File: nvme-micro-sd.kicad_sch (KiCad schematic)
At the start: 31 parts, among them J6 MicroSD_1140084168, J7 Bus_M.2_1-2199230-6, M2 Mech_M2_2280_H2.5mm

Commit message: [#54617] Review requested changes
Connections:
- net GND: no longer J6.10 (CD2), R?.1, R?.1
- new net: J6.10 (CD2), R?.1, R?.1
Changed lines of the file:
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@@
     (comment 1 "www.antmicro.com")
   )
-  (junction (at 236.22 222.25) (diameter 0) (color 0 0 0 0)
-  )
   (junction (at 224.79 46.99) (diameter 0) (color 0 0 0 0)
   )
@@
     (stroke (width 0) (type default))
   )
-  (wire (pts (xy 236.22 222.25) (xy 236.22 224.79))
-    (stroke (width 0) (type default))
-  )
   (wire (pts (xy 217.17 59.69) (xy 220.98 59.69))
     (stroke (width 0) (type default))
@@
     (stroke (width 0) (type default))
   )
-  (wire (pts (xy 236.22 212.09) (xy 236.22 222.25))
+  (wire (pts (xy 236.22 212.09) (xy 236.22 224.79))
     (stroke (width 0) (type default))
   )
@@
     (stroke (width 0) (type default))
   )
-  (wire (pts (xy 237.49 222.25) (xy 236.22 222.25))
-    (stroke (width 0) (type default))
-  )
   (wire (pts (xy 204.47 124.46) (xy 203.2 124.46))
     (stroke (width 0) (type default))
@@
     (stroke (width 0) (type default))
   )
-  (wire (pts (xy 228.6 222.25) (xy 236.22 222.25))
+  (wire (pts (xy 228.6 222.25) (xy 237.49 222.25))
     (stroke (width 0) (type default))
   )
@@
       (effects (font (size 1.27 1.27) (thickness 0.15)) (justify left bottom) hide)
     )
-    (property "Datasheet" " " (at 284.48 177.8 0)
+    (property "Datasheet" "https://product.tdk.com/en/search/capacitor/ceramic/mlcc/info?part_no=C1005X6S1A105K050BC" (at 284.48 177.8 0)
       (effects (font (size 1.27 1.27) (thickness 0.15)) (justify left bottom) hide)
     )
@@
   (symbol (lib_id "antmicropower:+3V3") (at 203.2 185.42 0) (unit 1)
     (in_bom yes) (on_board yes) (dnp no) (fields_autoplaced)
-    (property "Reference" "#PWR?" (at 218.44 187.96 0)
+    (property "Reference" "#PWR0206" (at 218.44 187.96 0)
       (effects (font (size 1.27 1.27) (thickness 0.15)) (justify left bottom) hide)
     )
@@
       (project "cm4-baseboard"
         (path "/60b842dc-0853-4a25-99ac-5784ddf94d0d/00000000-0000-0000-0000-00005fea1b94"
-          (reference "#PWR?") (unit 1)
+          (reference "#PWR0206") (unit 1)
         )
       )
@@
   (symbol (lib_id "antmicropower:GND") (at 269.24 199.39 0) (unit 1)
     (in_bom yes) (on_board yes) (dnp no)
-    (property "Reference" "#PWR?" (at 278.13 201.93 0)
+    (property "Reference" "#PWR0213" (at 278.13 201.93 0)
       (effects (font (size 1.27 1.27) (thickness 0.15)) (justify left bottom) hide)
     )
@@
       (project "cm4-baseboard"
         (path "/60b842dc-0853-4a25-99ac-5784ddf94d0d/00000000-0000-0000-0000-00005fea1b94"
-          (reference "#PWR?") (unit 1)
+          (reference "#PWR0213") (unit 1)
         )
       )
@@
       (effects (font (size 1.524 1.524)) (justify left bottom) hide)
     )
-    (property "Datasheet" " " (at 260.35 54.61 0)
+    (property "Datasheet" "https://product.tdk.com/en/search/capacitor/ceramic/mlcc/info?part_no=C1005X6S1A105K050BC" (at 260.35 54.61 0)
       (effects (font (size 1.27 1.27)) (justify left bottom) hide)
     )
@@
   (symbol (lib_id "antmicropower:+3V3") (at 236.22 185.42 0) (unit 1)
     (in_bom yes) (on_board yes) (dnp no) (fields_autoplaced)
-    (property "Reference" "#PWR?" (at 251.46 187.96 0)
+    (property "Reference" "#PWR0207" (at 251.46 187.96 0)
       (effects (font (size 1.27 1.27) (thickness 0.15)) (justify left bottom) hide)
     )
@@
       (project "cm4-baseboard"
         (path "/60b842dc-0853-4a25-99ac-5784ddf94d0d/00000000-0000-0000-0000-00005fea1b94"
-          (reference "#PWR?") (unit 1)
+          (reference "#PWR0207") (unit 1)
         )
       )
@@
   (symbol (lib_id "antmicropower:GND") (at 261.62 224.79 0) (unit 1)
     (in_bom yes) (on_board yes) (dnp no) (fields_autoplaced)
-    (property "Reference" "#PWR?" (at 270.51 227.33 0)
+    (property "Reference" "#PWR0212" (at 270.51 227.33 0)
       (effects (font (size 1.27 1.27) (thickness 0.15)) (justify left bottom) hide)
     )
@@
       (project "cm4-baseboard"
         (path "/60b842dc-0853-4a25-99ac-5784ddf94d0d/00000000-0000-0000-0000-00005fea1b94"
-          (reference "#PWR?") (unit 1)
+          (reference "#PWR0212") (unit 1)
         )
       )
@@
   (symbol (lib_id "antmicropower:GND") (at 151.13 210.82 0) (mirror y) (unit 1)
     (in_bom yes) (on_board yes) (dnp no) (fields_autoplaced)
-    (property "Reference" "#PWR?" (at 142.24 213.36 0)
+    (property "Reference" "#PWR0210" (at 142.24 213.36 0)
       (effects (font (size 1.27 1.27) (thickness 0.15)) (justify left bottom) hide)
     )
@@
       (project "cm4-baseboard"
         (path "/60b842dc-0853-4a25-99ac-5784ddf94d0d/00000000-0000-0000-0000-00005fea1b94"
-          (reference "#PWR?") (unit 1)
+          (reference "#PWR0210") (unit 1)
         )
       )
@@
       (effects (font (size 1.524 1.524)) (justify left bottom) hide)
     )
-    (property "Datasheet" " " (at 242.57 54.61 0)
+    (property "Datasheet" "https://product.tdk.com/en/search/capacitor/ceramic/mlcc/info?part_no=C1005X6S1A105K050BC" (at 242.57 54.61 0)
       (effects (font (size 1.27 1.27)) (justify left bottom) hide)
     )
@@
   (symbol (lib_id "antmicropower:GND") (at 228.6 231.14 0) (unit 1)
     (in_bom yes) (on_board yes) (dnp no) (fields_autoplaced)
-    (property "Reference" "#PWR?" (at 237.49 233.68 0)
+    (property "Reference" "#PWR0211" (at 237.49 233.68 0)
       (effects (font (size 1.27 1.27) (thickness 0.15)) (justify left bottom) hide)
     )
@@
       (project "cm4-baseboard"
         (path "/60b842dc-0853-4a25-99ac-5784ddf94d0d/00000000-0000-0000-0000-00005fea1b94"
-          (reference "#PWR?") (unit 1)
+          (reference "#PWR0211") (unit 1)
         )
       )
@@
       (effects (font (size 1.524 1.524)) (justify left bottom) hide)
     )
-    (property "Datasheet" " " (at 224.79 54.61 0)
+    (property "Datasheet" "https://product.tdk.com/en/search/capacitor/ceramic/mlcc/info?part_no=C1005X6S1A105K050BC" (at 224.79 54.61 0)
       (effects (font (size 1.27 1.27)) (justify left bottom) hide)
     )
@@
   (symbol (lib_id "antmicropower:+3V3") (at 151.13 195.58 0) (mirror y) (unit 1)
     (in_bom yes) (on_board yes) (dnp no) (fields_autoplaced)
-    (property "Reference" "#PWR?" (at 135.89 198.12 0)
+    (property "Reference" "#PWR0205" (at 135.89 198.12 0)
       (effects (font (size 1.27 1.27) (thickness 0.15)) (justify left bottom) hide)
     )
@@
       (project "cm4-baseboard"
         (path "/60b842dc-0853-4a25-99ac-5784ddf94d0d/00000000-0000-0000-0000-00005fea1b94"
-          (reference "#PWR?") (unit 1)
+          (reference "#PWR0205") (unit 1)
         )
       )
@@
       (effects (font (size 1.27 1.27) (thickness 0.15)) (justify left bottom) hide)
     )
-    (property "Datasheet" "https://pl.mouser.com/datasheet/2/916/PUSB3F96-1600324.pdf" (at 124.46 212.09 0)
+    (property "Datasheet" "https://mouser.com/datasheet/2/916/PUSB3F96-1600324.pdf" (at 124.46 212.09 0)
       (effects (font (size 1.27 1.27) (thickness 0.15)) (justify left bottom) hide)
     )
@@
       (effects (font (size 1.27 1.27) (thickness 0.15)) (justify left bottom) hide)
     )
-    (property "Datasheet" "https://pl.mouser.com/datasheet/2/916/PUSB3F96-1600324.pdf" (at 124.46 234.95 0)
+    (property "Datasheet" "https://mouser.com/datasheet/2/916/PUSB3F96-1600324.pdf" (at 124.46 234.95 0)
       (effects (font (size 1.27 1.27) (thickness 0.15)) (justify left bottom) hide)
     )
@@
   (symbol (lib_id "antmicropower:GND") (at 266.7 121.92 0) (mirror y) (unit 1)
     (in_bom yes) (on_board yes) (dnp no) (fields_autoplaced)
-    (property "Reference" "#PWR?" (at 257.81 124.46 0)
+    (property "Reference" "#PWR0208" (at 257.81 124.46 0)
       (effects (font (size 1.27 1.27) (thickness 0.15)) (justify left bottom) hide)
     )
@@
       (project "cm4-baseboard"
         (path "/60b842dc-0853-4a25-99ac-5784ddf94d0d/00000000-0000-0000-0000-00005fea1b94"
-          (reference "#PWR?") (unit 1)
+          (reference "#PWR0208") (unit 1)
         )
       )
@@
   (symbol (lib_id "antmicropower:GND") (at 151.13 233.68 0) (mirror y) (unit 1)
     (in_bom yes) (on_board yes) (dnp no) (fields_autoplaced)
-    (property "Reference" "#PWR?" (at 142.24 236.22 0)
+    (property "Reference" "#PWR0209" (at 142.24 236.22 0)
       (effects (font (size 1.27 1.27) (thickness 0.15)) (justify left bottom) hide)
     )
@@
       (project "cm4-baseboard"
         (path "/60b842dc-0853-4a25-99ac-5784ddf94d0d/00000000-0000-0000-0000-00005fea1b94"
-          (reference "#PWR?") (unit 1)
+          (reference "#PWR0209") (unit 1)
         )
       )
@@
   (symbol (lib_id "antmicropower:+3V3") (at 269.24 191.77 0) (unit 1)
     (in_bom yes) (on_board yes) (dnp no) (fields_autoplaced)
-    (property "Reference" "#PWR?" (at 284.48 194.31 0)
+    (property "Reference" "#PWR0214" (at 284.48 194.31 0)
       (effects (font (size 1.27 1.27) (thickness 0.15)) (justify left bottom) hide)
     )
@@
       (project "cm4-baseboard"
         (path "/60b842dc-0853-4a25-99ac-5784ddf94d0d/00000000-0000-0000-0000-00005fea1b94"
-          (reference "#PWR?") (unit 1)
+          (reference "#PWR0214") (unit 1)
         )
       )

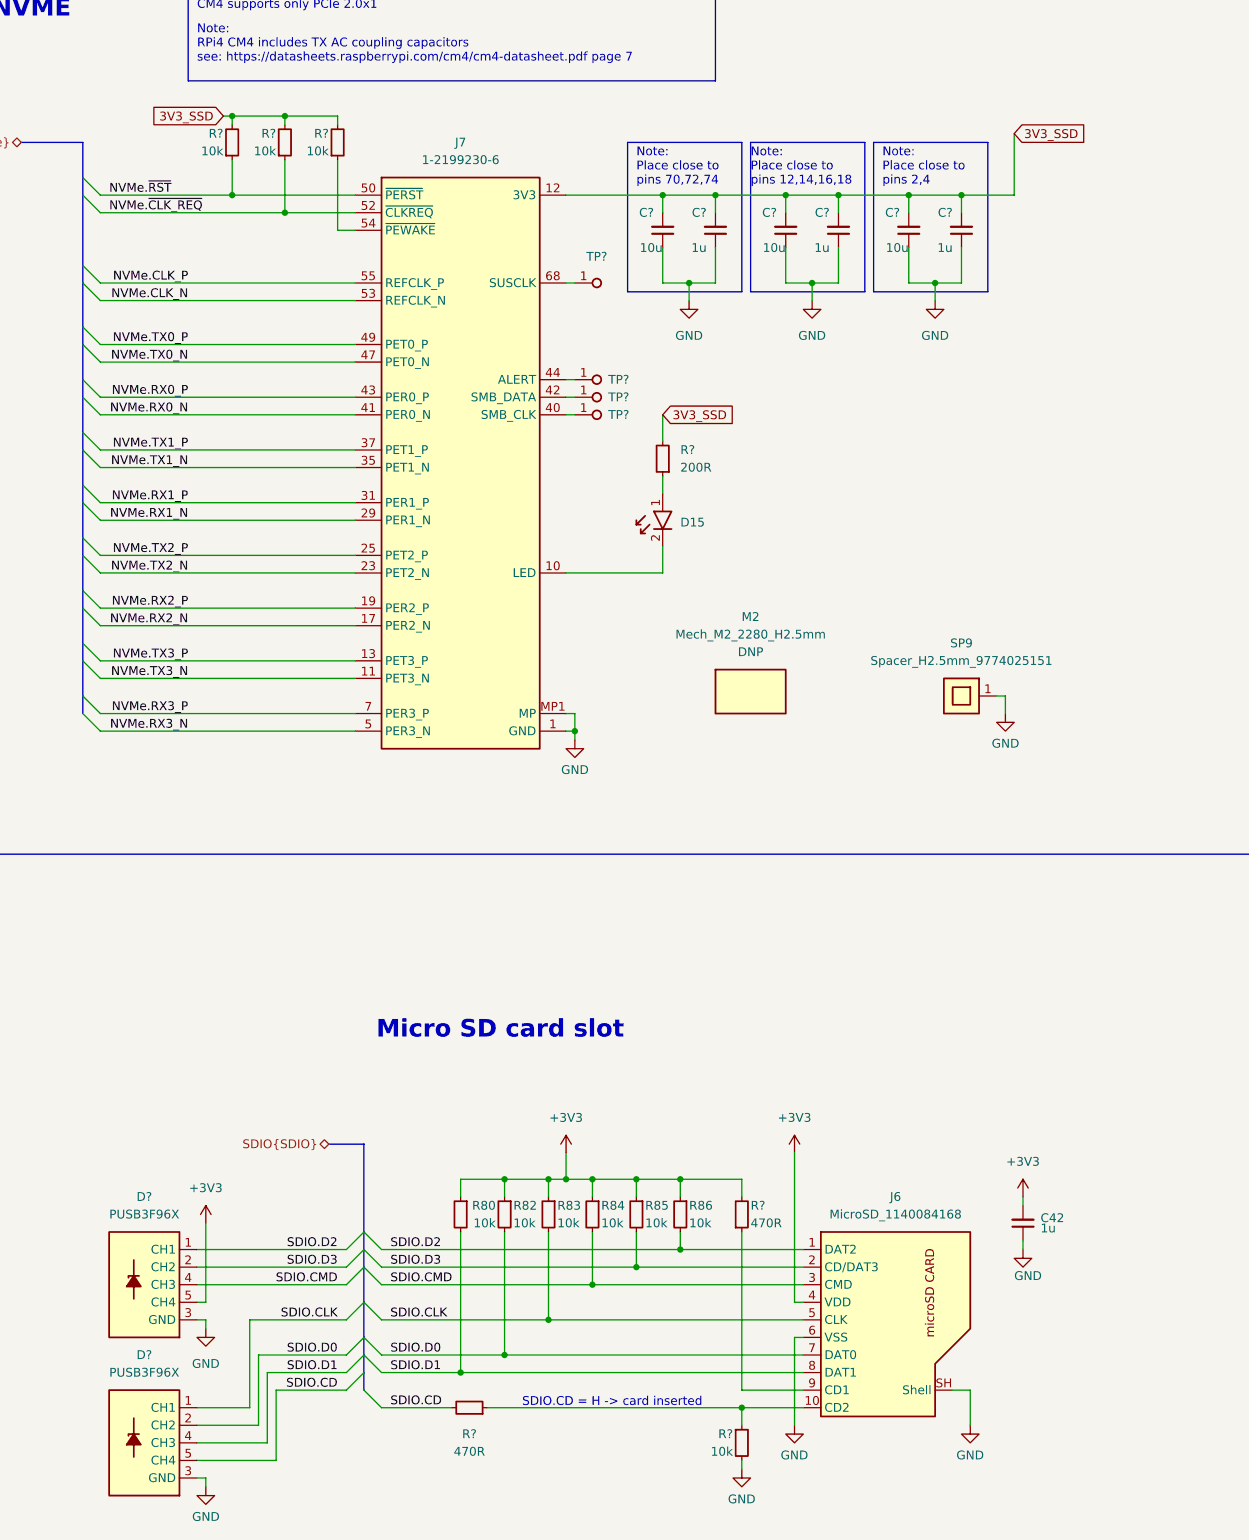
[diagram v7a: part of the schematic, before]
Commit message: [#54617] Re-enumerate reference designators
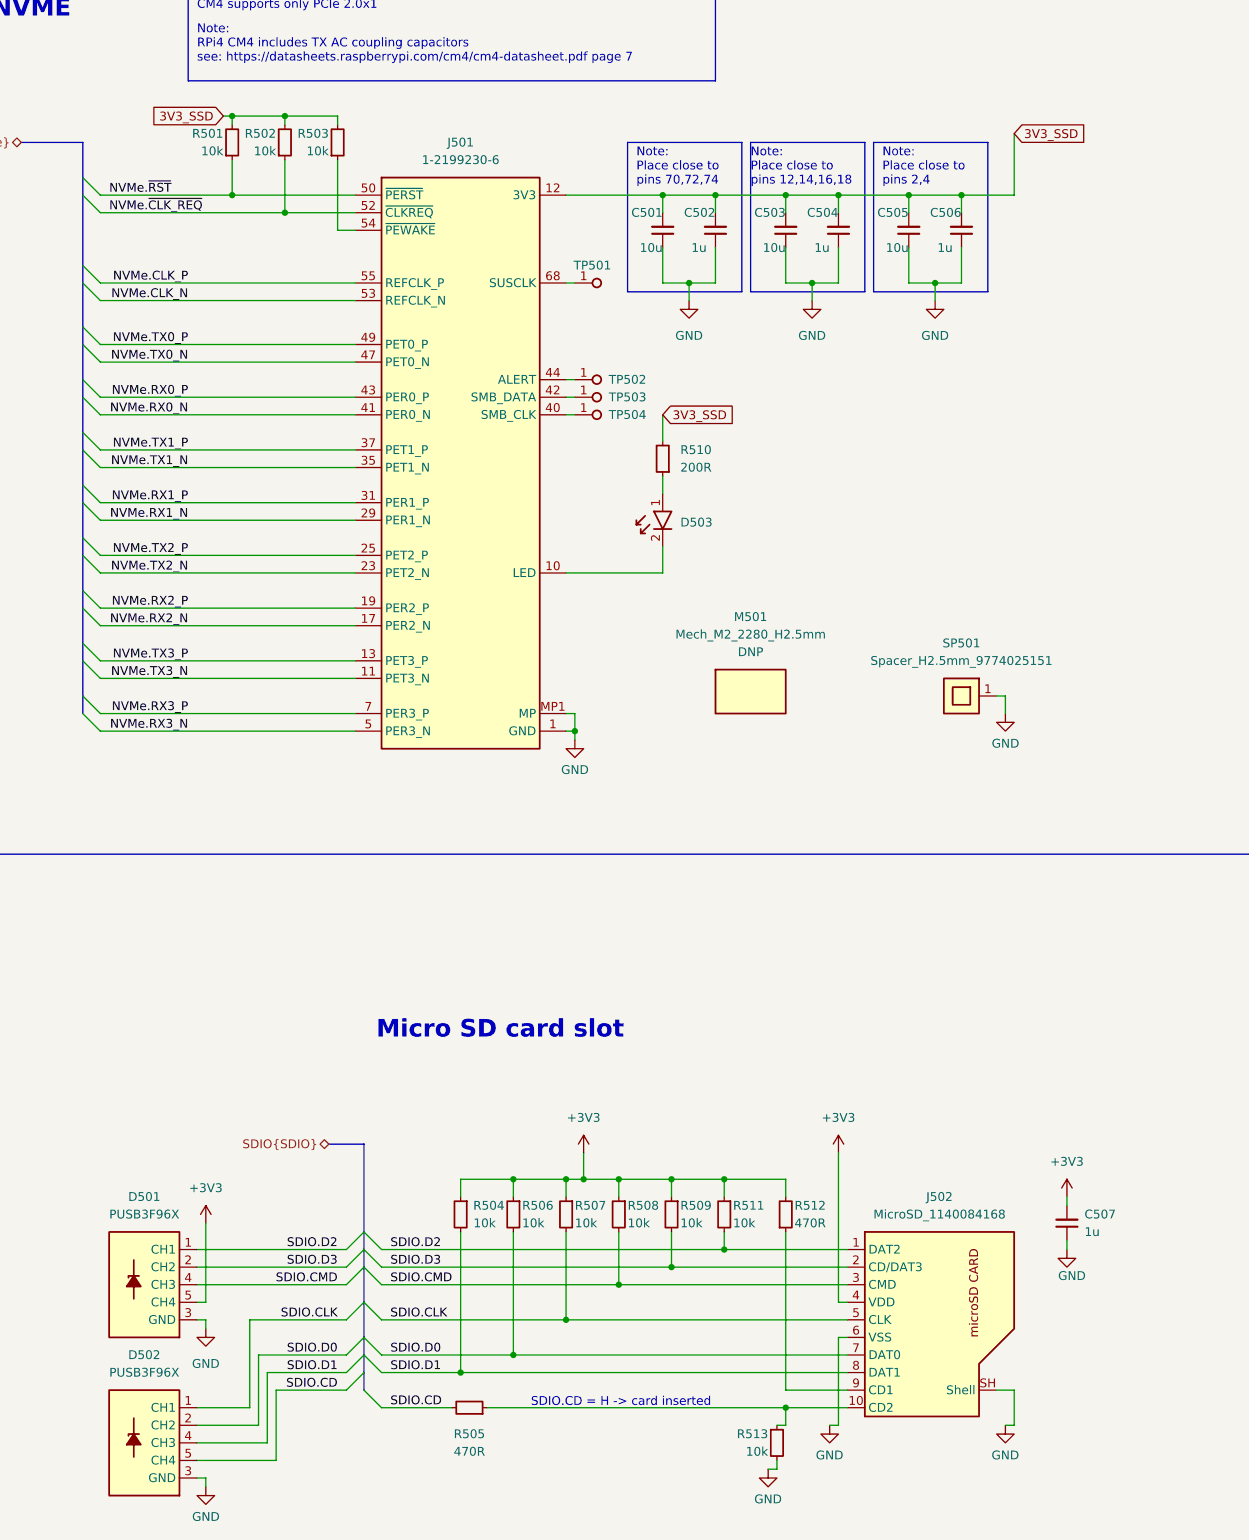
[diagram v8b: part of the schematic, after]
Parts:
- gave numbers to parts that had none: 19
- renumbered C42 to C507, D15 to D503, J7 to J501, J6 to J502, M2 to M501, R80 to R504, R82 to R506, R83 to R507, R84 to R508, R85 to R509, R86 to R511, SP9 to SP501
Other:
- moved on the sheet: C507, J502, R506, R507, R508, R509, R511, R512, R513
